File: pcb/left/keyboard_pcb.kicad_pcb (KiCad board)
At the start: 2 copper layers, 138.8 x 89.9 mm, 47 parts, among them J1 TRRS, J2 Conn_01x04_Male, K0 KEYSW, K1 KEYSW, K10 KEYSW, K11 KEYSW, K12 KEYSW, K13 KEYSW, K14 KEYSW, K15 KEYSW, K2 KEYSW, K20 KEYSW, K21 KEYSW, K22 KEYSW, K23 KEYSW, K24 KEYSW, K25 KEYSW, K3 KEYSW, K30 KEYSW, K31 KEYSW, K32 KEYSW, K4 KEYSW, K5 KEYSW, U1 PCF8574, U2 Pico

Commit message: first layout left
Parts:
- C1: value C -> 10uF
- C2: value C -> 100nF
- moved R1 42.2 mm to (194.8, 65.8), turned to -90 degrees
- moved R2 42.1 mm to (194.8, 69.5), turned to -90 degrees
- moved C2 21.4 mm to (107.2, 103.0), turned to 180 degrees
- moved C1 20.0 mm to (107.2, 104.8), turned to 180 degrees
- moved R5 15.0 mm to (112.0, 103.8), turned to -90 degrees
- moved D2 12.5 mm to (130.8, 110.8), turned to -90 degrees
- moved R4 8.00 mm to (126.3, 100.5), turned to 180 degrees
- moved D1 7.93 mm to (126.5, 107.0), turned to -90 degrees
- moved R3 7.79 mm to (126.4, 103.2), turned to 180 degrees
- moved R6 5.74 mm to (126.5, 110.5), turned to 90 degrees
- moved R7 3.95 mm to (130.8, 114.5), turned to 90 degrees
- moved U1 3.30 mm to (109.0, 109.5), turned to 90 degrees
- moved J1 0.94 mm to (202.1, 109.5)
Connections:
- U1 pad 4: /k00 -> /k20
- U1 pad 6: /k20 -> /k00
- U2 pad 10: /k23 -> /k14
- U2 pad 11: unconnected-(U2-Pad11) -> /k13
- U2 pad 12: unconnected-(U2-Pad12) -> /k12
- U2 pad 14: unconnected-(U2-Pad14) -> /k11
- U2 pad 15: unconnected-(U2-Pad15) -> /k01
- U2 pad 16: unconnected-(U2-Pad16) -> /k23
- U2 pad 17: /k24 -> /k25
- U2 pad 19: /k13 -> /k22
- U2 pad 20: /k03 -> /k24
- U2 pad 21: /k15 -> /k21
- U2 pad 22: /k14 -> /I2C_Int
- U2 pad 24: /k12 -> unconnected-(U2-Pad24)
- U2 pad 25: /k21 -> unconnected-(U2-Pad25)
- U2 pad 26: /k11 -> unconnected-(U2-Pad26)
- U2 pad 27: /I2C_Int -> unconnected-(U2-Pad27)
- U2 pad 29: /k01 -> unconnected-(U2-Pad29)
- U2 pad 6: /k25 -> /k03
- U2 pad 9: /k22 -> /k15
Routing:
- net VCC: track 0.00 -> 168.3 mm, vias 0 -> 4
- net /k21: track 0.00 -> 143.2 mm
- net /SCL: track 0.00 -> 127.4 mm, vias 1 -> 0
- net /SDA: track 0.00 -> 126.3 mm
- net /k01: track 0.00 -> 123.7 mm
- net /k13: track 0.00 -> 122.1 mm
- net /I2C_Int: track 0.00 -> 114.2 mm, vias 0 -> 1
- net /k32: track 0.00 -> 109.0 mm
- net /k11: track 0.00 -> 106.6 mm
- net /k02: track 0.00 -> 102.6 mm
- net /k22: track 0.00 -> 93.5 mm
- net /k12: track 0.00 -> 93.5 mm
- net /k03: track 0.00 -> 85.7 mm
- net /k00: track 0.00 -> 85.4 mm
- net /k31: track 0.00 -> 85.1 mm
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
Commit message: Added changes on the left board
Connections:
- U2 pad 11: /k13 -> unconnected-(U2-Pad11)
- U2 pad 12: /k12 -> unconnected-(U2-Pad12)
- U2 pad 14: /k11 -> /SDA
- U2 pad 15: /k01 -> /SCL
- U2 pad 16: /k23 -> unconnected-(U2-Pad16)
- U2 pad 24: unconnected-(U2-Pad24) -> /k01
- U2 pad 25: unconnected-(U2-Pad25) -> /k11
- U2 pad 26: unconnected-(U2-Pad26) -> /k23
- U2 pad 31: /SDA -> /k13
- U2 pad 32: /SCL -> /k12
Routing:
- net VCC: track 168.3 -> 0.00 mm, vias 4 -> 0
- net /k21: track 143.2 -> 0.00 mm
- net /SCL: track 127.4 -> 0.00 mm
- net /SDA: track 126.3 -> 0.00 mm
- net /k01: track 123.7 -> 0.00 mm
- net /k13: track 122.1 -> 0.00 mm
- net /I2C_Int: track 114.2 -> 0.00 mm, vias 1 -> 0
- net /k32: track 109.0 -> 0.00 mm
- net /k11: track 106.6 -> 0.00 mm
- net /k02: track 102.6 -> 0.00 mm
- net /k22: track 93.5 -> 0.00 mm
- net /k12: track 93.5 -> 0.00 mm
- net /k03: track 85.7 -> 0.00 mm
- net /k00: track 85.4 -> 0.00 mm
- net /k31: track 85.1 -> 0.00 mm
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
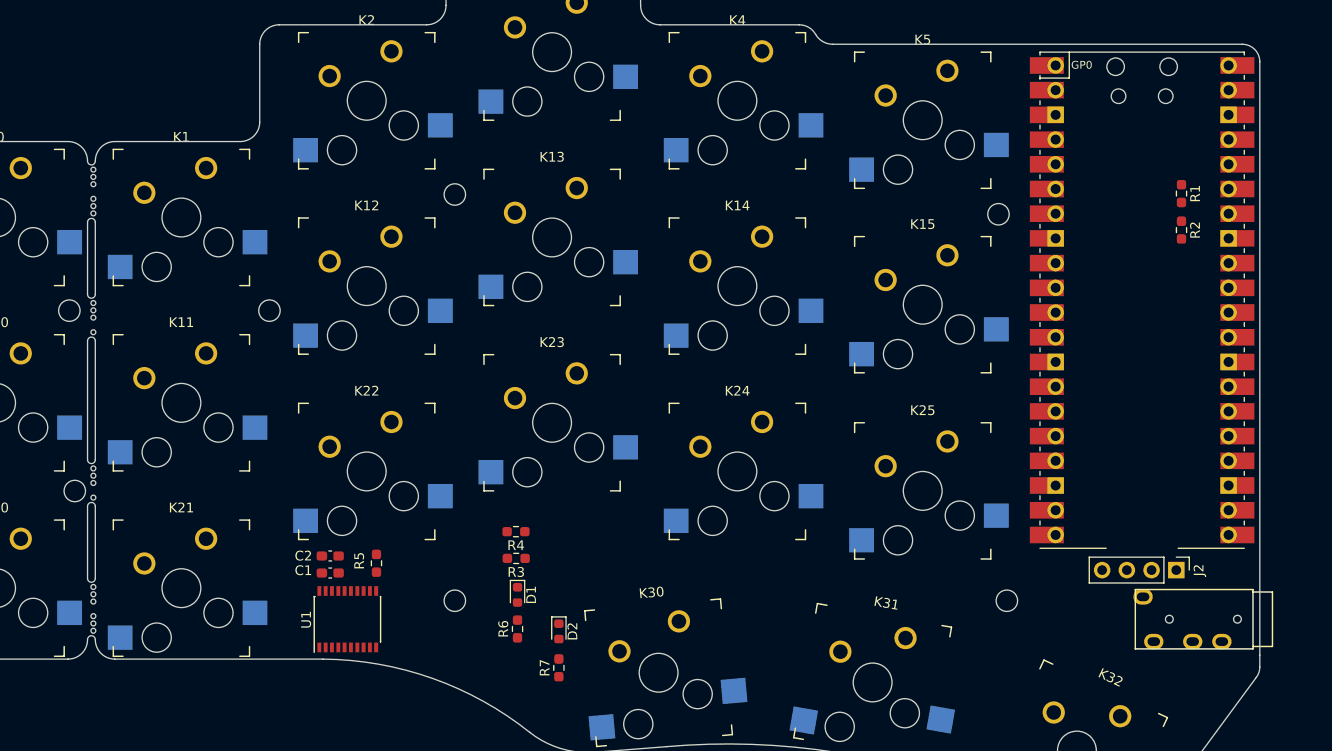
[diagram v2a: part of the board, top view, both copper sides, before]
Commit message: Mechanical parts are "mirrored", ToDo: Pin header LCD i2c pinheader needs alignment
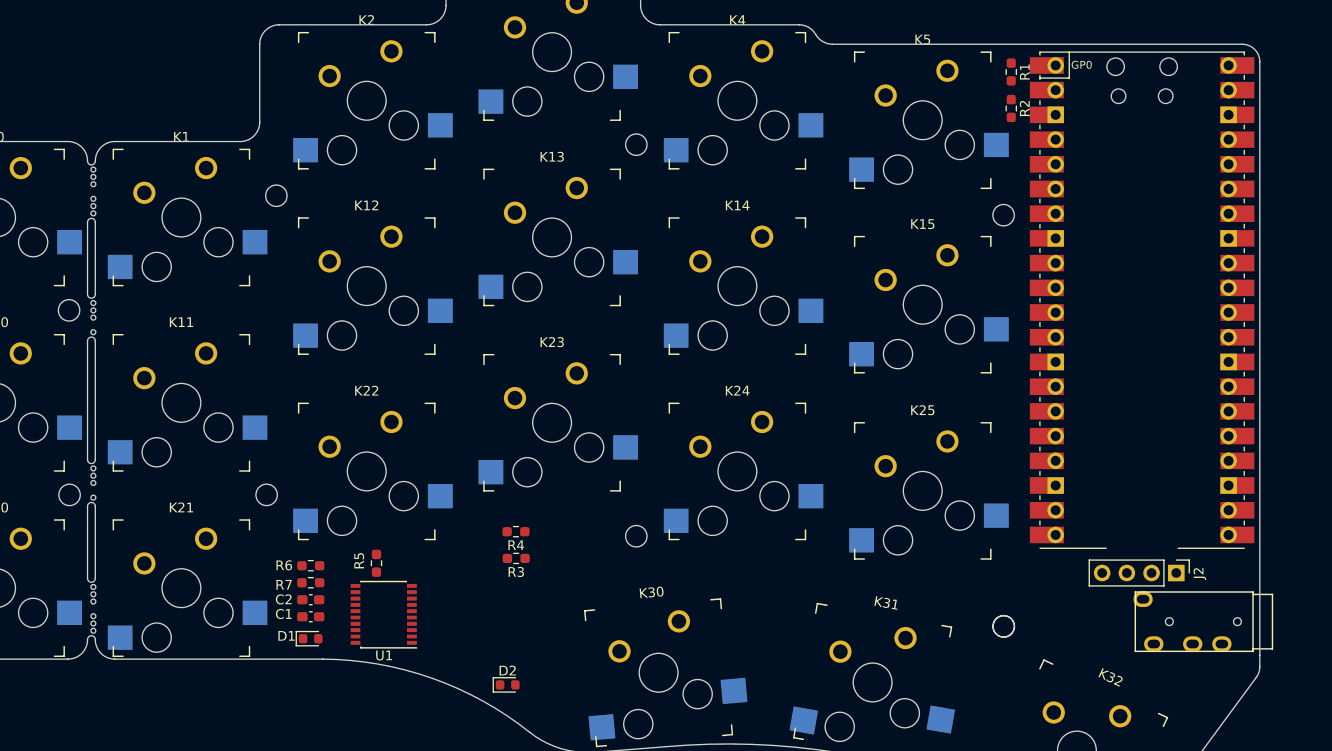
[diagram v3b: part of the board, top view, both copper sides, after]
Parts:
- removed the H1 at (120.1, 65.8)
- removed the H1 at (101.0, 77.8)
- removed the H4 at (120.1, 107.6)
- removed the H4 at (80.9, 96.3)
- removed the H4 at (80.4, 77.8)
- added H1: MountingHole, beekeeb_lib:MountingHole_2.2mm_M2-8mm, F.Cu at (101.7, 66.0)
- added H1: MountingHole, beekeeb_lib:MountingHole_2.2mm_M2-8mm, F.Cu at (138.7, 60.7)
- added H3: MountingHole, beekeeb_lib:MountingHole_2.2mm_M2-8mm, F.Cu at (176.5, 110.2)
- added H4: MountingHole, beekeeb_lib:MountingHole_2.2mm_M2-8mm, F.Cu at (138.7, 101.0)
- added H4: MountingHole, beekeeb_lib:MountingHole_2.2mm_M2-8mm, F.Cu at (100.7, 96.7)
- added H4: MountingHole, beekeeb_lib:MountingHole_2.2mm_M2-8mm, F.Cu at (80.4, 96.7)
- added H4: MountingHole, beekeeb_lib:MountingHole_2.2mm_M2-8mm, F.Cu at (80.4, 77.8)
- moved R7 27.0 mm to (105.2, 105.8), turned to 180 degrees
- moved R6 22.2 mm to (105.2, 104.0), turned to 180 degrees
- moved D1 21.7 mm to (105.2, 111.5), turned to 0 degrees
- moved R1 21.5 mm to (177.2, 53.2)
- moved R2 21.5 mm to (177.2, 57.0)
- moved D2 7.61 mm to (125.5, 116.2), turned to 0 degrees
- moved C1 4.92 mm to (105.2, 109.2)
- moved C2 4.92 mm to (105.2, 107.5)
- moved U1 3.72 mm to (112.7, 109.0), turned to 180 degrees
- moved H3 2.67 mm to (176.5, 110.2)
- moved H2 0.53 mm to (176.5, 68.0)
- moved J2 0.30 mm to (194.2, 104.8)
- moved J1 0.25 mm to (202.1, 109.8)

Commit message: Minor changes
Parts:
- removed the H3 at (176.5, 110.2)
- added SW1: SW_SPDT, Jumper:SolderJumper-3_P1.3mm_Open_RoundedPad1.0x1.5mm_NumberLabels, B.Cu at (193.2, 71.8)
- added SW2: SW_SPDT, Jumper:SolderJumper-3_P1.3mm_Open_RoundedPad1.0x1.5mm_NumberLabels, B.Cu at (193.2, 68.8)
- R3, R4: footprint Resistor_SMD:R_0603_1608Metric_Pad0.98x0.95mm_HandSolder -> Resistor_SMD:R_1206_3216Metric
- U1: value PCF8574 -> PCF8574TS/3
- moved R4 7.03 mm to (120.2, 104.0), turned to -90 degrees
- moved R3 3.45 mm to (123.0, 104.0), turned to -90 degrees
- moved C1 1.25 mm to (106.5, 109.2)
- moved C2 1.25 mm to (106.5, 107.5)
- moved R6 1.25 mm to (106.5, 104.0)
- moved R7 1.25 mm to (106.5, 105.8)
- turned D1 to 180 degrees
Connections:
- J1 pad 1: rx -> Net-(J1-SLEEVE)
- J1 pad 4: tx -> Net-(J1-RING2)
- U1 pad 7: /k31 -> /k30
- U1 pad 9: /k30 -> /k31
- U2 pad 17: /k25 -> /k13
- U2 pad 19: /k22 -> /k12
- U2 pad 20: /k24 -> /k25
- U2 pad 24: /k01 -> /k22
- U2 pad 31: /k13 -> /k24
- U2 pad 32: /k12 -> /k01
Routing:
- net /k01: track 0.00 -> 185.6 mm
- net VCC: track 0.00 -> 175.6 mm, vias 0 -> 5
- net /k11: track 0.00 -> 144.6 mm
- net /k21: track 0.00 -> 129.1 mm, vias 0 -> 1
- net /k22: track 0.00 -> 117.3 mm
- net /I2C_Int: track 0.00 -> 116.9 mm, vias 0 -> 1
- net /SDA: track 0.00 -> 115.6 mm, vias 0 -> 2
- net /k23: track 0.00 -> 108.7 mm
- net /SCL: track 0.00 -> 105.9 mm, vias 0 -> 2
- net GND: track 0.00 -> 103.2 mm, vias 0 -> 49
- net /k12: track 0.00 -> 99.6 mm
- net /k02: track 0.00 -> 94.6 mm
- net /k32: track 0.00 -> 94.4 mm
- net /k24: track 0.00 -> 92.4 mm
- net /k00: track 0.00 -> 91.4 mm, vias 0 -> 1
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- added copper zone on F.Cu, net VCC
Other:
- board text added: "LEFT"

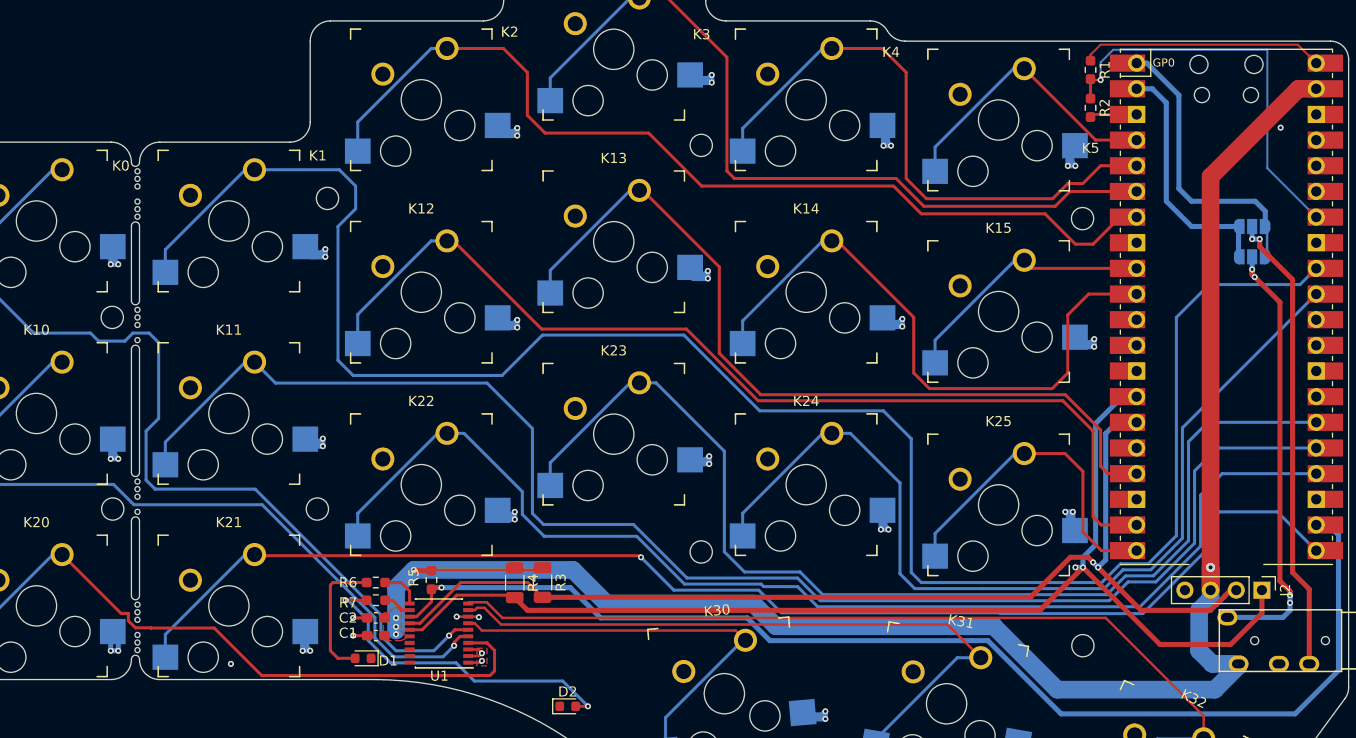
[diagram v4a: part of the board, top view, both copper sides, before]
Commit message: Left keyboard: Jumper to switch RX/TX direction removed in schematic and pcb.
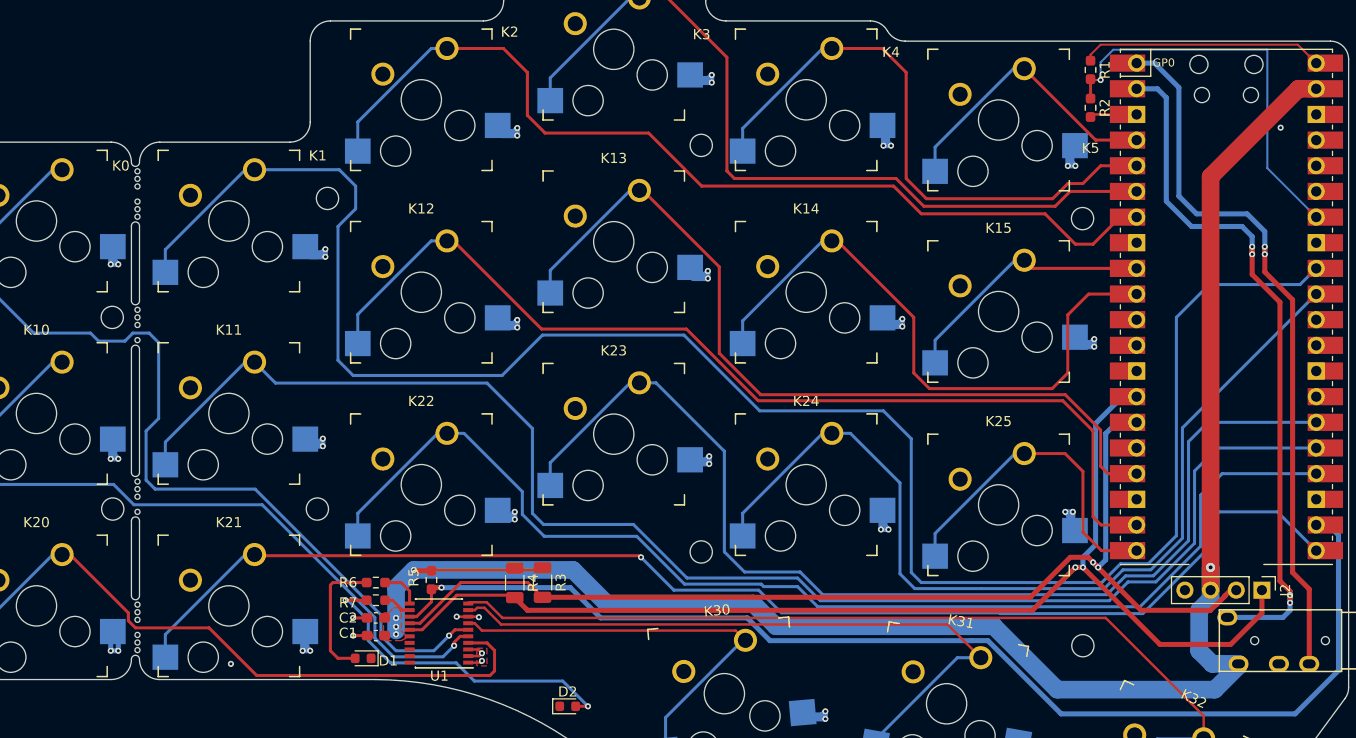
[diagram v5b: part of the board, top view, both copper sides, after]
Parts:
- removed SW1, SW2: SW_SPDT, Jumper:SolderJumper-3_P1.3mm_Open_RoundedPad1.0x1.5mm_NumberLabels
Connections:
- J1 pad 1: Net-(J1-SLEEVE) -> rx
- J1 pad 4: Net-(J1-RING2) -> tx
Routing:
- net rx: track 24.5 -> 70.8 mm, vias 0 -> 4
- net Net-(J1-RING2): track 46.1 -> 0.00 mm, vias 2 -> 0
- net Net-(J1-SLEEVE): track 43.9 -> 0.00 mm, vias 4 -> 0
- net tx: track 28.9 -> 71.3 mm, vias 0 -> 2
- net /SCL: track 105.9 -> 106.6 mm

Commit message: finetuning regarding BOM and part placement
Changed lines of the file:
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@@
     (fp_line (start 1.6 0.8) (end -1.6 0.8)
       (stroke (width 0.1) (type solid)) (layer "F.Fab"))
-    (pad "1" smd roundrect (at -1.4625 0 270) (size 1.125 1.75) (layers "F.Cu" "F.Paste" "F.Mask") (roundrect_rratio 0.222222)
+    (pad "1" smd roundrect (at -1.4625 0 270) (size 1.125 1.75) (layers "F.Cu" "F.Paste" "F.Mask") (roundrect_rratio 0.2222222222)
       (net 31 "VCC") (pintype "passive"))
-    (pad "2" smd roundrect (at 1.4625 0 270) (size 1.125 1.75) (layers "F.Cu" "F.Paste" "F.Mask") (roundrect_rratio 0.222222)
+    (pad "2" smd roundrect (at 1.4625 0 270) (size 1.125 1.75) (layers "F.Cu" "F.Paste" "F.Mask") (roundrect_rratio 0.2222222222)
       (net 29 "/SCL") (pintype "passive"))
     (model "${KICAD6_3DMODEL_DIR}/Resistor_SMD.3dshapes/R_1206_3216Metric.wrl"
@@
     (fp_line (start 1.6 0.8) (end -1.6 0.8)
       (stroke (width 0.1) (type solid)) (layer "F.Fab"))
-    (pad "1" smd roundrect (at -1.4625 0 270) (size 1.125 1.75) (layers "F.Cu" "F.Paste" "F.Mask") (roundrect_rratio 0.222222)
+    (pad "1" smd roundrect (at -1.4625 0 270) (size 1.125 1.75) (layers "F.Cu" "F.Paste" "F.Mask") (roundrect_rratio 0.2222222222)
       (net 31 "VCC") (pintype "passive"))
-    (pad "2" smd roundrect (at 1.4625 0 270) (size 1.125 1.75) (layers "F.Cu" "F.Paste" "F.Mask") (roundrect_rratio 0.222222)
+    (pad "2" smd roundrect (at 1.4625 0 270) (size 1.125 1.75) (layers "F.Cu" "F.Paste" "F.Mask") (roundrect_rratio 0.2222222222)
       (net 28 "/SDA") (pintype "passive"))
     (model "${KICAD6_3DMODEL_DIR}/Resistor_SMD.3dshapes/R_1206_3216Metric.wrl"

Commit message: v1.0
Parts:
- K0, K1, K10, K11, K12, K13, K14, K15, K2, K20, K21, K22, K23, K24, K25, K3, K30, K31, K32, K4, K5: footprint keyswitches:Kailh_socket_MX_optional_platemount -> keyswitches:Kailh_socket_MX_optional_platemount_3d_pretty_by_datasheet
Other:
- board text added: "Left"
- board text added: "Piantor_MX"
- board text added: "v1.0"

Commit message: Revision 1.1 WIP#
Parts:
- removed J2: Conn_01x04_Male, Connector_PinHeader_2.54mm:PinHeader_1x04_P2.54mm_Vertical
- removed MB1, MB2: MountingHole, beekeeb_lib:mousebites_2
- removed MB3, MB4: MountingHole, beekeeb_lib:mousebites_3
- added R10: 10k, Resistor_SMD:R_0603_1608Metric_Pad0.98x0.95mm_HandSolder, F.Cu at (100.5, 105.1)
- added R11: 10k, Resistor_SMD:R_0603_1608Metric_Pad0.98x0.95mm_HandSolder, F.Cu at (108.0, 105.2)
- added R12: 10k, Resistor_SMD:R_0603_1608Metric_Pad0.98x0.95mm_HandSolder, F.Cu at (130.8, 118.5)
- added R13: 10k, Resistor_SMD:R_0603_1608Metric_Pad0.98x0.95mm_HandSolder, F.Cu at (150.5, 108.8)
- added R14: 10k, Resistor_SMD:R_0603_1608Metric_Pad0.98x0.95mm_HandSolder, B.Cu at (186.2, 88.9)
- added R8: 10k, Resistor_SMD:R_0603_1608Metric_Pad0.98x0.95mm_HandSolder, F.Cu at (106.2, 105.2)
- added R9: 10k, Resistor_SMD:R_0603_1608Metric_Pad0.98x0.95mm_HandSolder, F.Cu at (104.5, 105.2)
- added TP1: TestPoint, TestPoint:TestPoint_Pad_D3.0mm, F.Cu at (2.02, 2.02)
- added U3: PCF8574TS, Package_SO:SSOP-20_4.4x6.5mm_P0.65mm, B.Cu at (188.5, 66.2)
- C1, C2: moved to B.Cu
- H1, H6, H7, H8: renamed from H4; footprint beekeeb_lib:MountingHole_2.2mm_M2-8mm -> misc:MountingHole_2.2mm_M2-8mm
- H2, H3: renamed from H1; footprint beekeeb_lib:MountingHole_2.2mm_M2-8mm -> misc:MountingHole_2.2mm_M2-8mm
- H4: renamed from H2; footprint beekeeb_lib:MountingHole_2.2mm_M2-8mm -> misc:MountingHole_2.2mm_M2-8mm
- H5: renamed from H3; footprint beekeeb_lib:MountingHole_2.2mm_M2-8mm -> misc:MountingHole_2.2mm_M2-8mm
- R3, R4: value R -> 4k7; footprint Resistor_SMD:R_1206_3216Metric -> Resistor_SMD:R_0603_1608Metric_Pad0.98x0.95mm_HandSolder; moved to B.Cu
- U1: value PCF8574TS/3 -> MCP23009-E/SO; footprint Package_SO:SSOP-20_4.4x6.5mm_P0.65mm -> Package_SO:SOIC-18W_7.5x11.6mm_P1.27mm; moved to B.Cu
- U2: footprint RPi_Pico:RPi_Pico_SMD_TH -> misc:RPi_Pico_SMD_TH
- moved U1 82.9 mm to (189.4, 77.5), turned to 0 degrees
- moved R4 81.4 mm to (188.6, 59.8), turned to 180 degrees
- moved R3 75.0 mm to (184.8, 61.5), turned to 180 degrees
- moved C1 25.2 mm to (129.5, 99.0)
- moved R7 24.8 mm to (129.0, 116.2)
- moved C2 24.0 mm to (129.5, 100.5)
- moved R5 7.83 mm to (109.8, 111.2)
- moved R6 5.88 mm to (105.2, 109.8)
- moved H8 1.84 mm to (82.2, 97.0)
- moved H1 1.81 mm to (82.2, 77.8)
- moved H7 0.40 mm to (101.0, 97.0)
- moved H2 0.36 mm to (102.0, 65.8)
- moved H4 0.27 mm to (176.5, 67.7)
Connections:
- C1 pad 1: VCC -> +3.3V
- C2 pad 1: VCC -> +3.3V
- R3 pad 1: VCC -> +3.3V
- R4 pad 1: VCC -> +3.3V
- R5 pad 1: VCC -> +3.3V
- U1 pad 1: GND -> +3.3V
- U1 pad 10: /k32 -> /k00
- U1 pad 11: /LED_A -> /k30
- U1 pad 12: /LED_B -> /k31
- U1 pad 13: /I2C_Int -> /k32
- U1 pad 14: /SCL -> /LED_A
- U1 pad 15: /SDA -> /LED_B
- U1 pad 16: VCC -> unconnected-(U1-NC-Pad16)
- U1 pad 17: (no net) -> unconnected-(U1-NC-Pad17)
- U1 pad 18: (no net) -> GND
- U1 pad 2: GND -> unconnected-(U1-NC-Pad2)
- U1 pad 3: GND -> /SCL
- U1 pad 4: /k20 -> /SDA
- U1 pad 5: /k10 -> GND
- U1 pad 6: /k00 -> /MCP_RST
- U1 pad 7: /k30 -> /I2C_Int
- U1 pad 8: GND -> /k20
- U1 pad 9: /k31 -> /k10
- U2 pad 14: /SDA -> unconnected-(U2-GPIO10-Pad14)
- U2 pad 15: /SCL -> unconnected-(U2-GPIO11-Pad15)
- U2 pad 27: unconnected-(U2-GPIO21-Pad27) -> /k24
- U2 pad 29: unconnected-(U2-GPIO22-Pad29) -> /k01
- U2 pad 31: /k24 -> /k04
- U2 pad 32: /k01 -> /k05
- U2 pad 36: unconnected-(U2-3V3-Pad36) -> +3.3V
- U2 pad 4: /k05 -> /SDA
- U2 pad 5: /k04 -> /SCL
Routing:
- net +3.3V: track 0.00 -> 194.4 mm, vias 0 -> 8
- net VCC: track 175.6 -> 50.7 mm, vias 5 -> 0
- net /k05: track 28.5 -> 114.6 mm
- net /SDA: track 115.6 -> 30.4 mm, vias 2 -> 3
- net /SCL: track 106.6 -> 27.2 mm, vias 2 -> 3
- net /k04: track 58.2 -> 128.9 mm
- net /k32: track 94.4 -> 24.4 mm
- net /k31: track 67.0 -> 20.3 mm
- net Net-(D2-A): track 32.8 -> 2.31 mm, vias 2 -> 0
- net /k20: track 67.7 -> 40.1 mm
- net /I2C_Int: track 116.9 -> 93.0 mm, vias 1 -> 0
- net /k30: track 42.5 -> 19.3 mm
- net /k01: track 185.6 -> 169.2 mm
- net /k00: track 91.4 -> 78.4 mm, vias 1 -> 0
- net Net-(D1-A): track 13.0 -> 0.00 mm
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- removed copper zone on F.Cu, net VCC
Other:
- outline, holes or cut-outs redrawn
- board text added: "v1.1"
- board text removed: "v1.0"
